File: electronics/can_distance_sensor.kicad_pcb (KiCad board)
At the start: 4 copper layers, 40.6 x 40.6 mm, 75 parts, among them J1 USB_B_Micro, J2 Conn_ARM_JTAG_SWD_10, J3 Conn_01x04, Q1 IRLML6401, SW1 PTS645SK50SMTR92LFS, U1 USBLC6-2SC6, U2 STM32G431CBUx, U3 TLV75801PDRV, U4 AOZ1280CI, U5 TLV75801PDRV, U6 TCAN1044A-Q1, U7 VL53L3CXV0DH/1, U8 TCA9509DGKR, Y1 Crystal_GND24

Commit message: Major refactor to rev B
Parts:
- removed C5, C6, C7: 0.1u, Capacitor_SMD:C_0402_1005Metric
- removed J1: USB_B_Micro, Connector_USB:USB_Micro-B_Amphenol_10118193-0001LF_Horizontal
- removed R1: 560, Resistor_SMD:R_0402_1005Metric
- removed U2: STM32G431CBUx, Package_DFN_QFN:QFN-48-1EP_7x7mm_P0.5mm_EP5.6x5.6mm
- added D8: SP0502BAHT, Package_TO_SOT_SMD:SOT-23, F.Cu at (176.8, 113.9)
- added D9: SP0502BAHT, Package_TO_SOT_SMD:SOT-23, F.Cu at (176.8, 109.8)
- added H1: MountingHole, MountingHole:MountingHole_2.2mm_M2, F.Cu at (181.0, 112.0)
- added H2: MountingHole, MountingHole:MountingHole_2.2mm_M2, F.Cu at (211.2, 117.0)
- added J4: Conn_01x06, Connector_JST:JST_PH_S6B-PH-K_1x06_P2.00mm_Horizontal, F.Cu at (172.0, 107.0)
- added J5: USB_C_Receptacle, footprints:CONN_105450-0101_MOL, F.Cu at (174.0, 98.0)
- added JP1: SolderJumper_3_Bridged12, Jumper:SolderJumper-3_P1.3mm_Bridged2Bar12_RoundedPad1.0x1.5mm_NumberLabels, F.Cu at (177.6, 106.0)
- added TP10: TestPoint, TestPoint:TestPoint_Pad_D1.0mm, B.Cu at (175.6, 115.6)
- added TP11: TestPoint, TestPoint:TestPoint_Pad_D1.0mm, B.Cu at (175.6, 118.1)
- added TP12: TestPoint, TestPoint:TestPoint_Pad_D1.0mm, B.Cu at (178.3, 115.6)
- added TP13: TestPoint, TestPoint:TestPoint_Pad_D1.0mm, B.Cu at (206.0, 94.4)
- added TP14: TestPoint, TestPoint:TestPoint_Pad_D1.0mm, B.Cu at (206.0, 91.9)
- added TP9: TestPoint, TestPoint:TestPoint_Pad_D1.0mm, B.Cu at (178.3, 118.1)
- added U9: STM32G0B1KBUx, Package_DFN_QFN:QFN-32-1EP_5x5mm_P0.5mm_EP3.45x3.45mm, F.Cu at (194.7, 94.7)
- moved C22 22.2 mm to (182.1, 115.5), turned to 0 degrees
- moved TP8 22.1 mm to (190.0, 98.0)
- moved R16 21.9 mm to (184.7, 114.3), turned to 0 degrees
- moved TP1 21.2 mm to (208.3, 108.9), turned to 180 degrees
- moved TP6 20.4 mm to (192.3, 98.0)
- moved R8 17.8 mm to (213.0, 93.3), turned to 0 degrees
- moved D6 13.7 mm to (183.4, 117.6)
- moved D2 13.4 mm to (210.2, 93.3), turned to 0 degrees
- moved TP7 13.3 mm to (187.7, 98.0)
- moved R17 12.9 mm to (184.7, 115.5)
- moved TP5 12.5 mm to (194.8, 98.0), turned to 180 degrees
- moved C3 12.3 mm to (199.8, 94.5), turned to 0 degrees
- moved R9 12.1 mm to (213.0, 91.6), turned to 0 degrees
- moved R7 12.0 mm to (199.8, 90.9), turned to 0 degrees
- moved D3 11.1 mm to (210.2, 91.6), turned to 0 degrees
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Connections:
- D7 pad 1: Net-(J3-Pin_3) -> Net-(J3-Pin_4)
- D7 pad 2: Net-(J3-Pin_4) -> Net-(J3-Pin_3)
- J2 pad 4: SWCLK -> BOOT
- TP1 pad 1: TOF_SDA -> GND
- TP2 pad 1: TOF_SCL -> VCC
- TP3 pad 1: TOF_INT -> 3V3
- TP4 pad 1: TOF_XSHUT -> 2V8
- TP5 pad 1: GND -> TOF_XSHUT
- TP6 pad 1: 3V3 -> TOF_INT
- TP7 pad 1: VCC -> TOF_SCL
- TP8 pad 1: 2V8 -> TOF_SDA
- U1 pad 4: Net-(R4-Pad1) -> Net-(R5-Pad1)
- U1 pad 6: Net-(R5-Pad1) -> Net-(R4-Pad1)
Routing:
- net TB_ABS: track 0.00 -> 75.8 mm, vias 0 -> 5
- net BOOT: track 30.0 -> 100.0 mm, vias 2 -> 5
- net TB_MOSI: track 0.00 -> 48.6 mm, vias 0 -> 1
- net TB_CS: track 0.00 -> 46.9 mm, vias 0 -> 5
- net TB_CLK: track 0.00 -> 42.6 mm, vias 0 -> 3
- net +12V: track 13.2 -> 49.0 mm, vias 0 -> 2
- net ID: track 28.9 -> 0.00 mm, vias 2 -> 0
- net Net-(J4-Pin_6): track 0.00 -> 23.6 mm, vias 0 -> 1
- net GND: track 49.1 -> 69.9 mm, vias 33 -> 53
- net SWCLK: track 19.6 -> 0.00 mm, vias 1 -> 0
- net LED2: track 4.96 -> 21.2 mm, vias 0 -> 2
- net 2V8: track 61.0 -> 45.2 mm, vias 2 -> 1
- net CAN_STB: track 12.9 -> 25.9 mm
- net VIN_MEAS: track 56.8 -> 45.5 mm
- net LED1: track 4.26 -> 13.6 mm, vias 0 -> 2
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- removed copper zone on B.Cu, net GND
- removed copper zone on F.Cu, net GND
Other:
- board size 40.6 x 40.6 mm -> 46 x 30 mm
- board text added: "TOF Utility Rev B Copyright 2025 Team 7048 & 4360"
- board text added: "TP1 = GND TP2 = +5V TP3 = +3.3V TP4 = 2.8V TP5 = TOF_XSHUT TP6 = TOF_INT TP7 = TOF_SCL TP8 = TOF_SDA TP9 = TB_CS TP10 = TB_MOSI TP11 = TB_MISO TP12 = TB_CLK"
- board text removed: "I'm Not Touching You Rev A Copyright 2024 Team 7048 & 4360"
- board text removed: "TP1 = 3.3V TP2 = TOF_SDA TP3 = VCC TP4 = TOF_SCL TP5 = TOF_INT TP6 = TOF_XSHUT TP7 = GND"

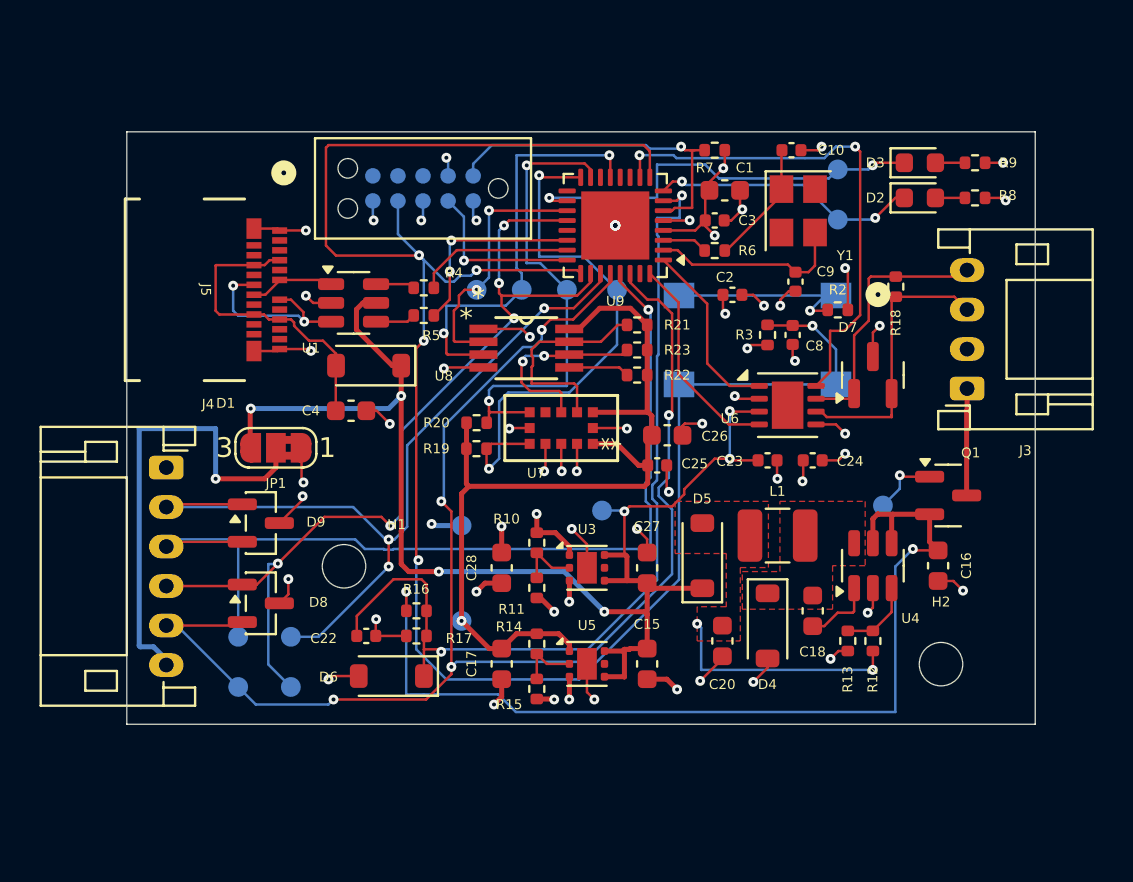
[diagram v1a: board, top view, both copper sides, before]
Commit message: Refactored the design to use basic parts.
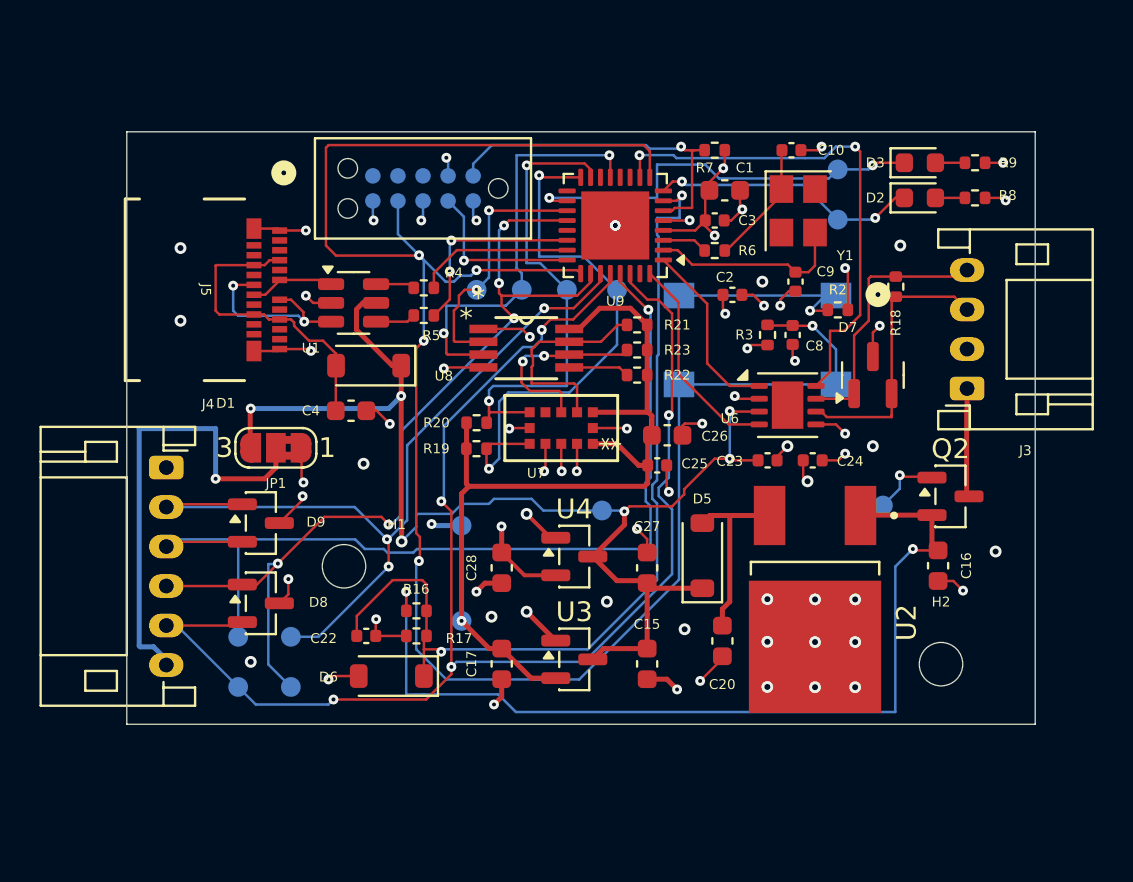
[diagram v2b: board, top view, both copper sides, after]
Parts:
- removed C18: 10n, Capacitor_SMD:C_0603_1608Metric
- removed D4: D_Schottky, Diode_SMD:D_SOD-123
- removed L1: L, Inductor_SMD:L_1210_3225Metric
- removed Q1: IRLML6401, Package_TO_SOT_SMD:SOT-23
- removed R10: 5k, Resistor_SMD:R_0402_1005Metric
- removed R11, R15: 1k, Resistor_SMD:R_0402_1005Metric
- removed R12: 49.9k, Resistor_SMD:R_0402_1005Metric
- removed R13: 9.53k, Resistor_SMD:R_0402_1005Metric
- removed R14: 4.09k, Resistor_SMD:R_0402_1005Metric
- removed U5: TLV75801PDRV, Package_SON:WSON-6-1EP_2x2mm_P0.65mm_EP1x1.6mm
- added Q2: AO3401A, Package_TO_SOT_SMD:SOT-23, F.Cu at (211.7, 108.5)
- added U2: L78M05ABDT-TR, footprints:VREG_L78M05ABDT-TR, F.Cu at (204.9, 113.7)
- U3: value TLV75801PDRV -> TPS7A0508PDBZ; footprint Package_SON:WSON-6-1EP_2x2mm_P0.65mm_EP1x1.6mm -> Package_TO_SOT_SMD:SOT-23
- U4: value AOZ1280CI -> TPS7A0508PDBZ; footprint Package_TO_SOT_SMD:SOT-23-6 -> Package_TO_SOT_SMD:SOT-23
- moved U4 15.1 mm to (192.7, 111.5), turned to 0 degrees
- moved U3 4.68 mm to (192.7, 116.7)
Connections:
- U3 pad 1: 3V3 -> GND
- U3 pad 2: Net-(U3-FB) -> 2V8
- U3 pad 3: GND -> VCC
- U4 pad 1: Net-(U4-BST) -> GND
- U4 pad 2: GND -> 3V3
- U4 pad 3: Net-(U4-FB) -> VCC
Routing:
- net GND: track 69.9 -> 61.7 mm, vias 53 -> 66
- net VCC: track 69.4 -> 64.2 mm, vias 7 -> 6
- net Net-(U4-FB): track 3.83 -> 0.00 mm
- net Net-(U4-BST): track 3.58 -> 0.00 mm
- net Net-(U3-FB): track 3.23 -> 0.00 mm
- net Net-(U5-FB): track 3.13 -> 0.00 mm
- net /Power/PRE_OUT: track 12.1 -> 9.30 mm, vias 2 -> 0
- net +12V: track 49.0 -> 46.8 mm
- net 2V8: track 45.2 -> 44.3 mm
- net 3V3: track 27.0 -> 26.9 mm, vias 14 -> 13
- removed copper zone on F.Cu, net /Power/LX
- removed copper zone on F.Cu, net /Power/PRE_OUT
